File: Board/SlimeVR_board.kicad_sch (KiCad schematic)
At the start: 36 parts, among them IC1 HT7833, J1 USB_C_Receptacle_USB2.0_16P, J2 Conn_01x02_Pin, J3 Conn_01x04_Pin, J5 Conn_01x01_Pin, J6 Conn_01x01_Pin, J7 Conn_01x04_Pin, Q1 DMP3099L, SW1 SW_SPDT, U1 TP4056-42-ESOP8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

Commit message: New Version
skiped few version that ware bad or not good or not funcioning
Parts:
- C1, C10, C2, C4, C5: Source (none) -> https://www.tme.eu/cz/details/0603b104k500ct/kondenzatory-m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
- C3, C6, C7, C8, C9: Source (none) -> https://www.tme.eu/cz/details/0201zd105mat2a/kondenzatory-m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
- D1: value LED -> FYLS-1206URC; Source (none) -> https://www.tme.eu/cz/details/fyls-1206urc/diody-led-smd-ba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
- D2: value LED -> FYLS-1206PGC; Source (none) -> https://www.tme.eu/cz/details/fyls-1206pgc/diody-led-smd-ba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
- D3: value LED -> FYLS-1206UWC; Source (none) -> https://www.tme.eu/cz/details/fyls-1206uwc/diody-led-smd-bi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
- D4: value D -> 1N4148WSQ-7-F; Source (none) -> https://www.tme.eu/cz/details/1n4148wsq-7-f/univerzalni-dio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
- IC1: Source (none) -> https://www.laskakit.cz/holtek-ht7833-3-3v-0-5a-stabilizato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
- J1: Source (none) -> https://www.tme.eu/cz/details/usb4105-gf-a/konektory-usb-a-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
- J2: value Conn_01x02_Pin -> JST-PH; Source (none) -> https://www.tme.eu/cz/details/b2b-ph-sm4-tb/signalove-konek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
- J3: value Conn_01x04_Pin -> SMD_Pads; footprint Connector_PinSocket_2.54mm:PinSocket_1x04_P2.54mm_Vertical -> Custom:Pin_1x04_SMD_P2.54mm
- J7: value Conn_01x04_Pin -> JTX-HX; Source (none) -> https://www.tme.eu/cz/details/s4b-xh-a-1/signalove-konektor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
- Q1: value DMP3099L -> DMP3099L-7; Source (none) -> https://www.tme.eu/cz/details/dmp3099l-7/tranzistory-s-kana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
- R1: value 10k -> 47k; Source (none) -> https://www.tme.eu/cz/details/0805s8f4702t5e/rezistory-smd/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
- R10, R9: Source (none) -> https://www.tme.eu/cz/details/smd0805-10k-1%25/rezistory-sm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
- R11, R3, R4: Source (none) -> https://www.tme.eu/cz/details/wr08x5101ftl/rezistory-smd/wa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
- R2: value 3k3 -> 47k; Source (none) -> https://www.tme.eu/cz/details/0805s8f4702t5e/rezistory-smd/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
- R5, R6, R8: Source (none) -> https://www.tme.eu/cz/details/smd0805-1k-1%25/rezistory-smd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
- R7: Source (none) -> https://www.tme.eu/cz/details/rca0805jk20tfea/rezistory-smd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
- SW1: value SW_SPDT -> LA215009; footprint Button_Switch_THT:SW_Slide_SPDT_Angled_CK_OS102011MA1Q -> Button_Switch_THT:SW_Slide-03_Wuerth-WS-SLTV_10x2.5x6.4_P2.54mm; Source (none) -> https://www.laskakit.cz/posuvny-prepinac-0-3a-50vdc/
- U1: Source (none) -> https://www.laskakit.cz/toppower-tp4056-nabijecka-li-ion-cl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
- U2: Source (none) -> https://www.tme.eu/cz/details/esp32c3-wroom-02n4/moduly-iot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

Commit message: New version
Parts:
- added J4: SMD_Pads, Custom:Pin_1x04_SMD_P2.54mm, symbol Connector:Conn_01x04_Pin
- added J8: JTX-HX-A-1, Connector_JST:JST_XH_S4B-XH-A-1_1x04_P2.50mm_Horizontal, symbol Connector:Conn_01x04_Pin
- J7: value JTX-HX -> JTX-HX-A-1; footprint Connector_JST:JST_XH_S4B-XH-A_1x04_P2.50mm_Horizontal -> Connector_JST:JST_XH_S4B-XH-A-1_1x04_P2.50mm_Horizontal
- U1: value TP4056-42-ESOP8 -> TP4056-ESOP8
- U2: value ESP32-C3-WROOM-02 -> ESP32-C3-WROOM-02-N4
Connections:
- net +3.3V: now also J4.1 (Pin_1), J8.4 (Pin_4)
- net Earth: now also J7.3 (Pin_3), J4.2 (Pin_2), J8.2 (Pin_2); no longer J7.2 (Pin_2)
- net Battery_sence: now reaches R1.1, R2.2, U2.15 (IO3)
- net SCL: now reaches J3.3 (Pin_3), U2.4 (IO5)
- net SCL: now also J7.2 (Pin_2), J4.3 (Pin_3), J8.3 (Pin_3); no longer J7.3 (Pin_3)
- net SDA: now reaches J3.4 (Pin_4), J7.4 (Pin_4), U2.3 (IO4)
- net SDA: now also J4.4 (Pin_4), J8.1 (Pin_1)
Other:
- note added: "Charging"
- note added: "Extencion IMU"
- note added: "From +Batt to 3.3V"
- note added: "Main IMU"
- note added: "Main MCU"
- note added: "USB-C"
- moved on the sheet: C1, C10, C2, C3, C4, C5, C6, C7, C8, C9, D1, D2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

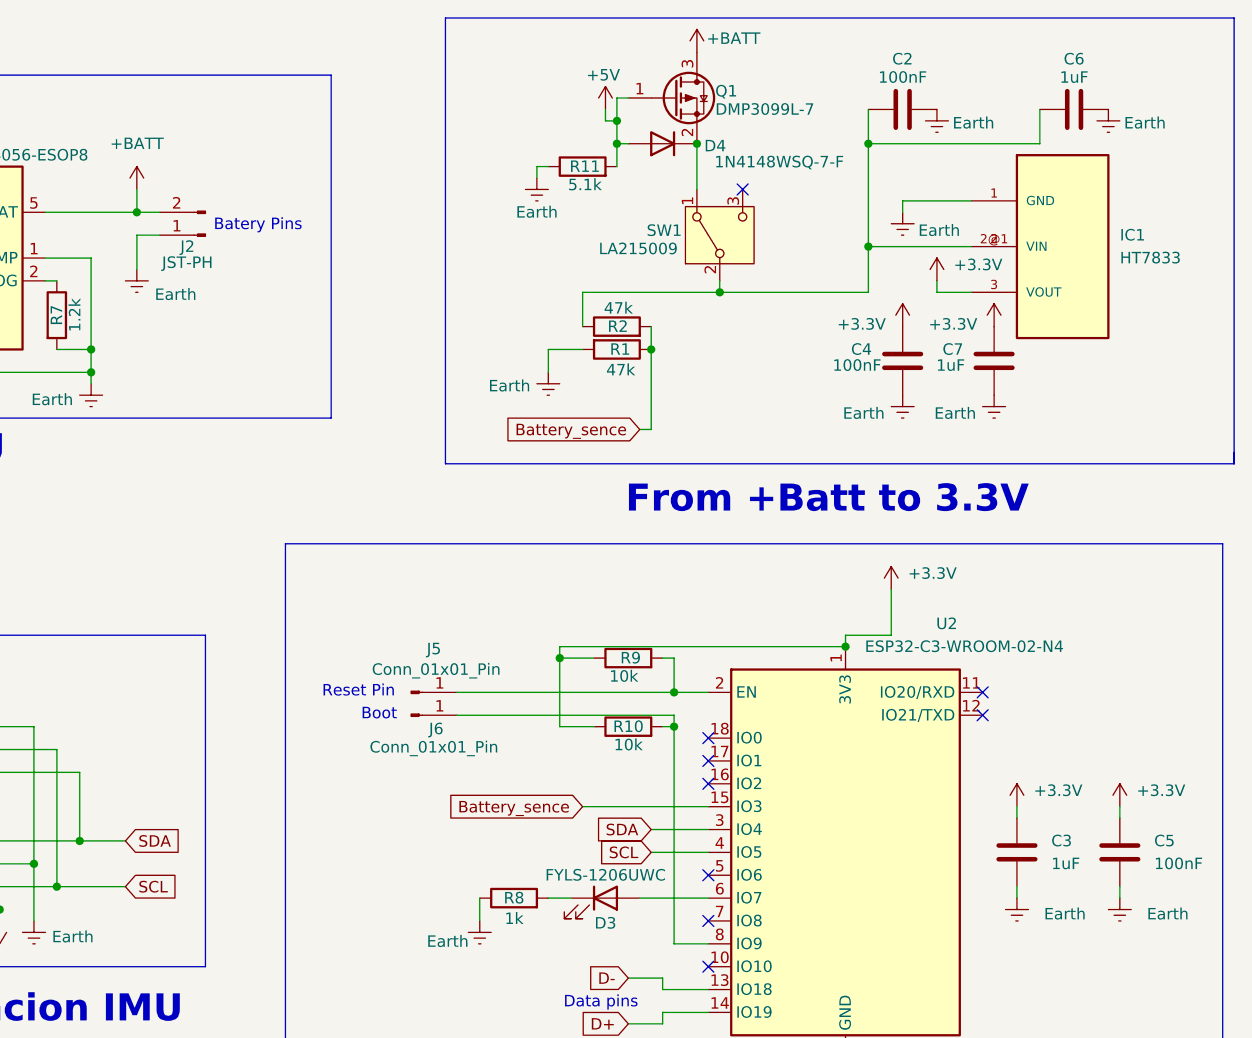
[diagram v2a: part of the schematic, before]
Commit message: New version of board
Fixex:
- grafical issues and speling
- wrong diode used, board wont get more then 150mA
- battery pins has been swaped for standarizes conection
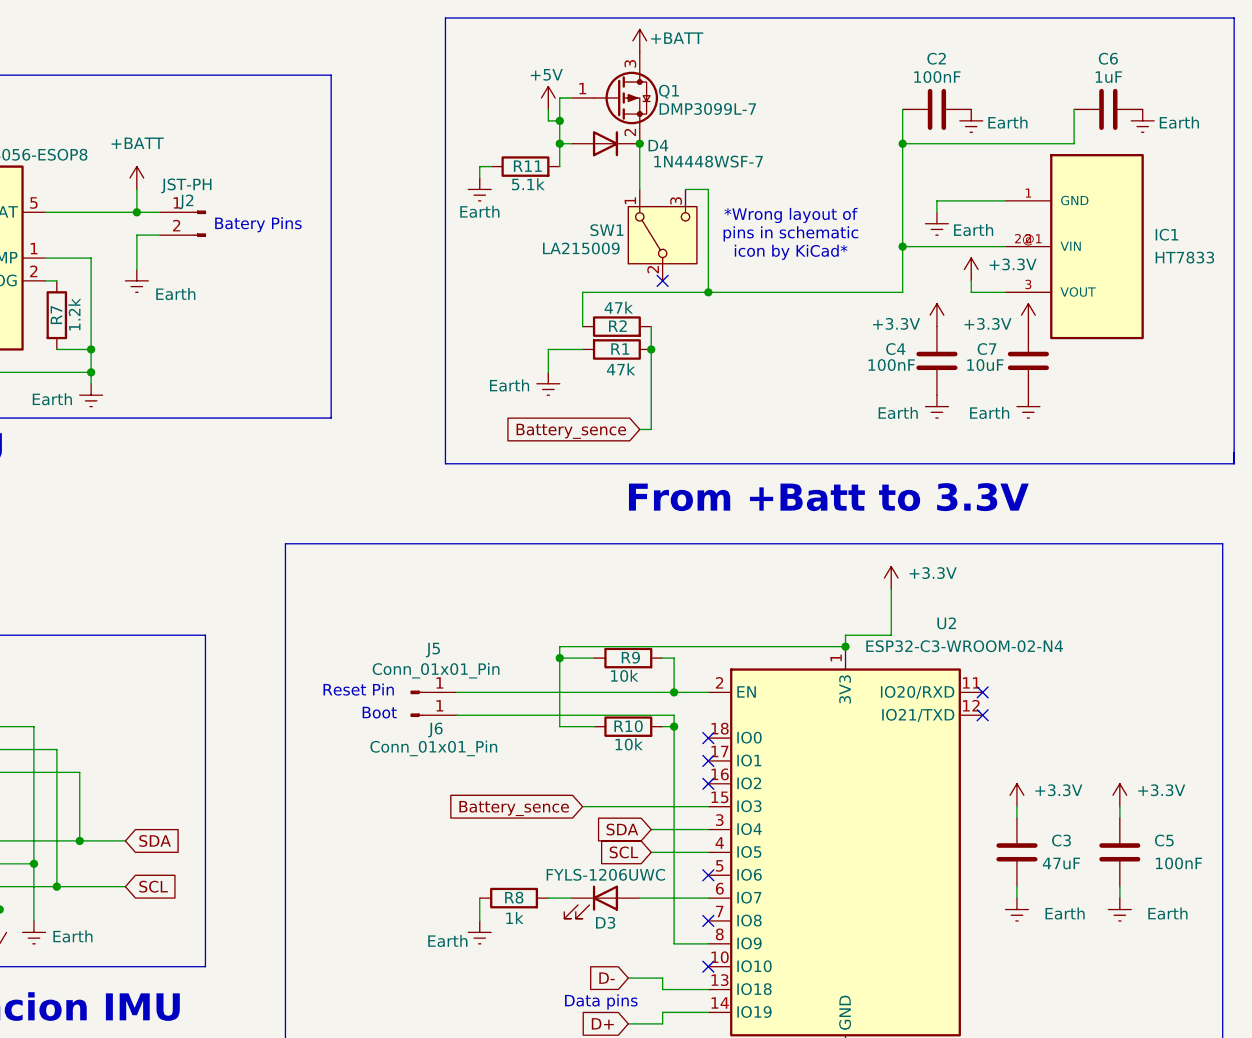
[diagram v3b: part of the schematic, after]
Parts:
- C3: value 1uF -> 47uF
- C7: value 1uF -> 10uF
- D4: value 1N4148WSQ-7-F -> 1N4448WSF-7
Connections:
- net +BATT: now also J2.1 (Pin_1); no longer J2.2 (Pin_2)
- net Earth: now also J2.2 (Pin_2); no longer J2.1 (Pin_1)
- net at C2.1, C6.1, IC1.2 (VIN)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: now also SW1.3 (C); no longer SW1.2 (B)
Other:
- note added: "*Wrong layout of pins in schematic icon by KiCad*"
- moved on the sheet: C2, C4, C6, C7, D4, IC1, J2, Q1, R11, SW1

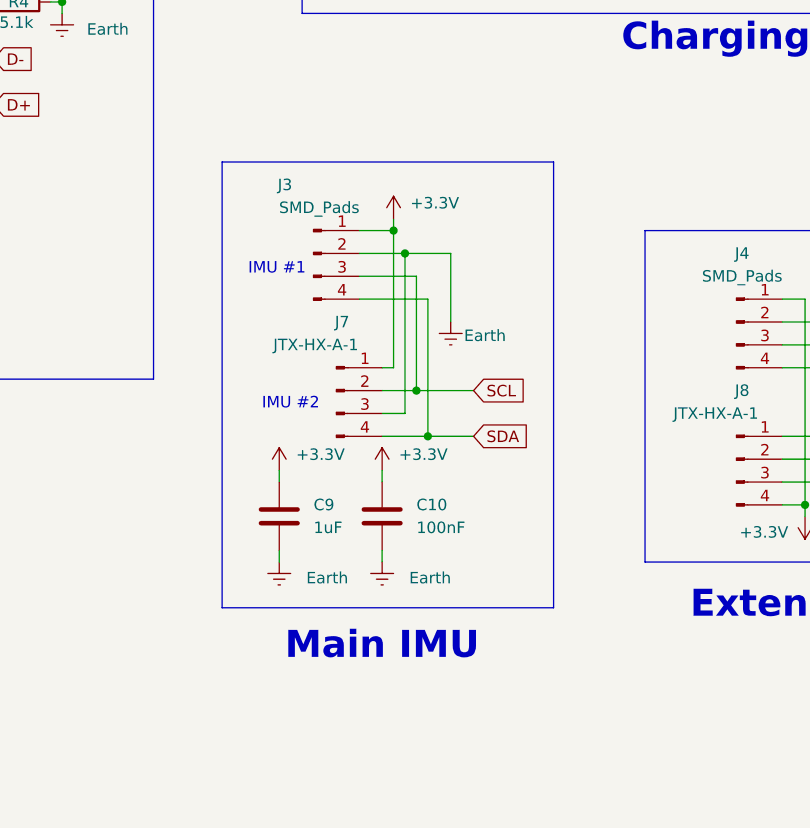
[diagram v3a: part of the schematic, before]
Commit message: Nweset Board update
Update log:
- Moved 3.3 conventor closer to esp for more stability
- Properly labeled Boot and Reset pads with own GND
- New and remade grafic
- Two capacitators no more needed (material saving :D)
- New Logo (I got some logo of my probebly will change idk)
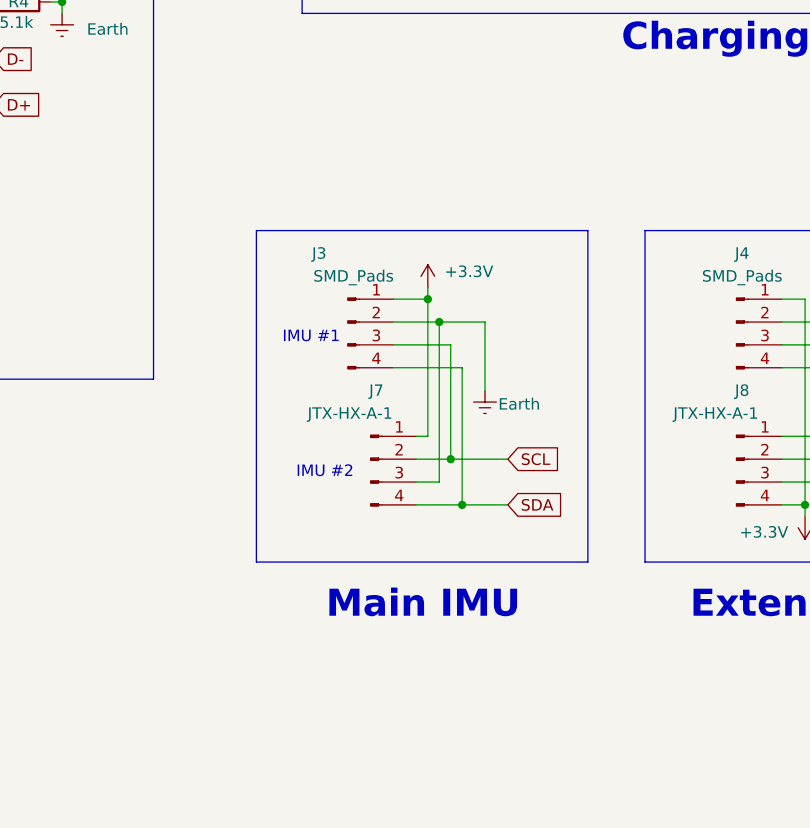
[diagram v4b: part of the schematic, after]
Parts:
- removed C10: 100nF, Capacitor_SMD:C_0603_1608Metric_Pad1.08x0.95mm_HandSolder, symbol Device:C
- removed C9: 1uF, Capacitor_SMD:C_0603_1608Metric_Pad1.08x0.95mm_HandSolder, symbol Device:C
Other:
- moved on the sheet: J3, J7
